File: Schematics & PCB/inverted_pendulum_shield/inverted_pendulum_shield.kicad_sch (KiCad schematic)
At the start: 6 parts, among them U1 AS78L05RTR-E1

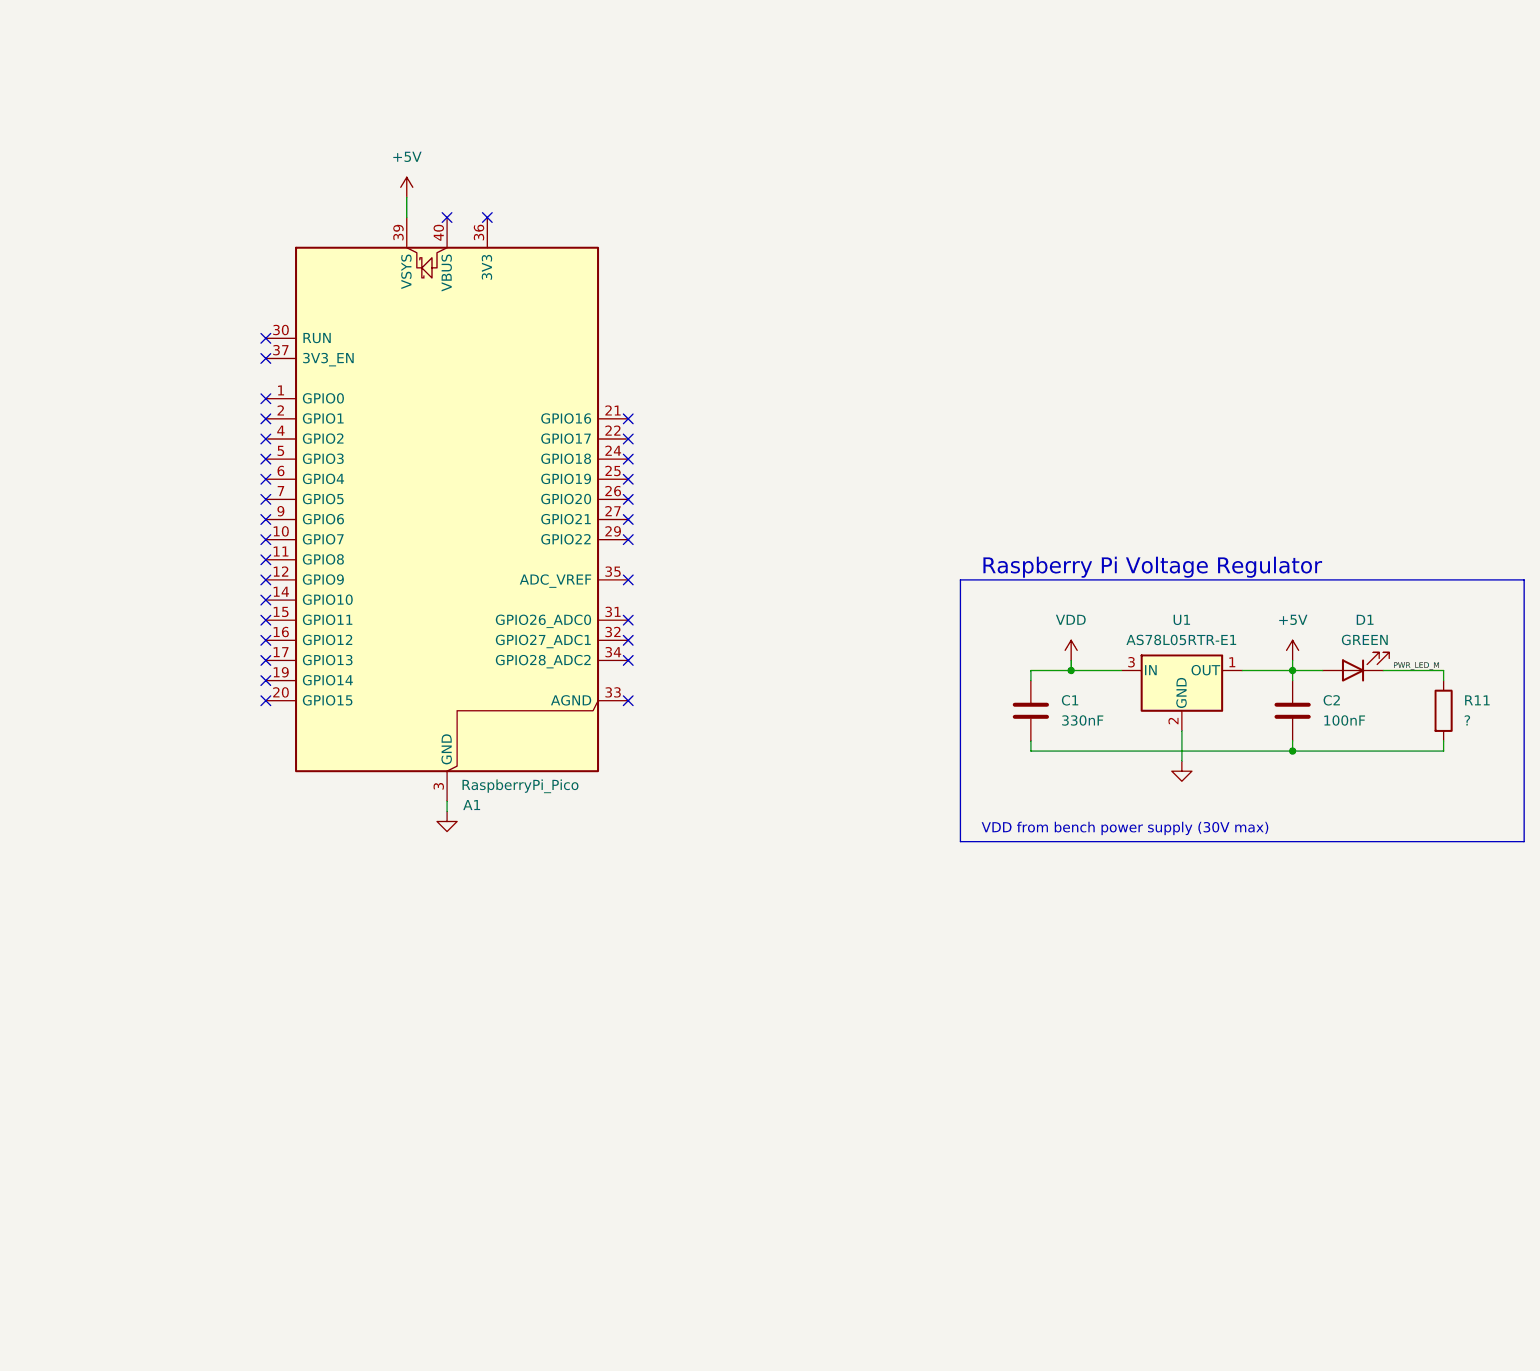
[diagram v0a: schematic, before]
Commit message: added reverse polarity protection
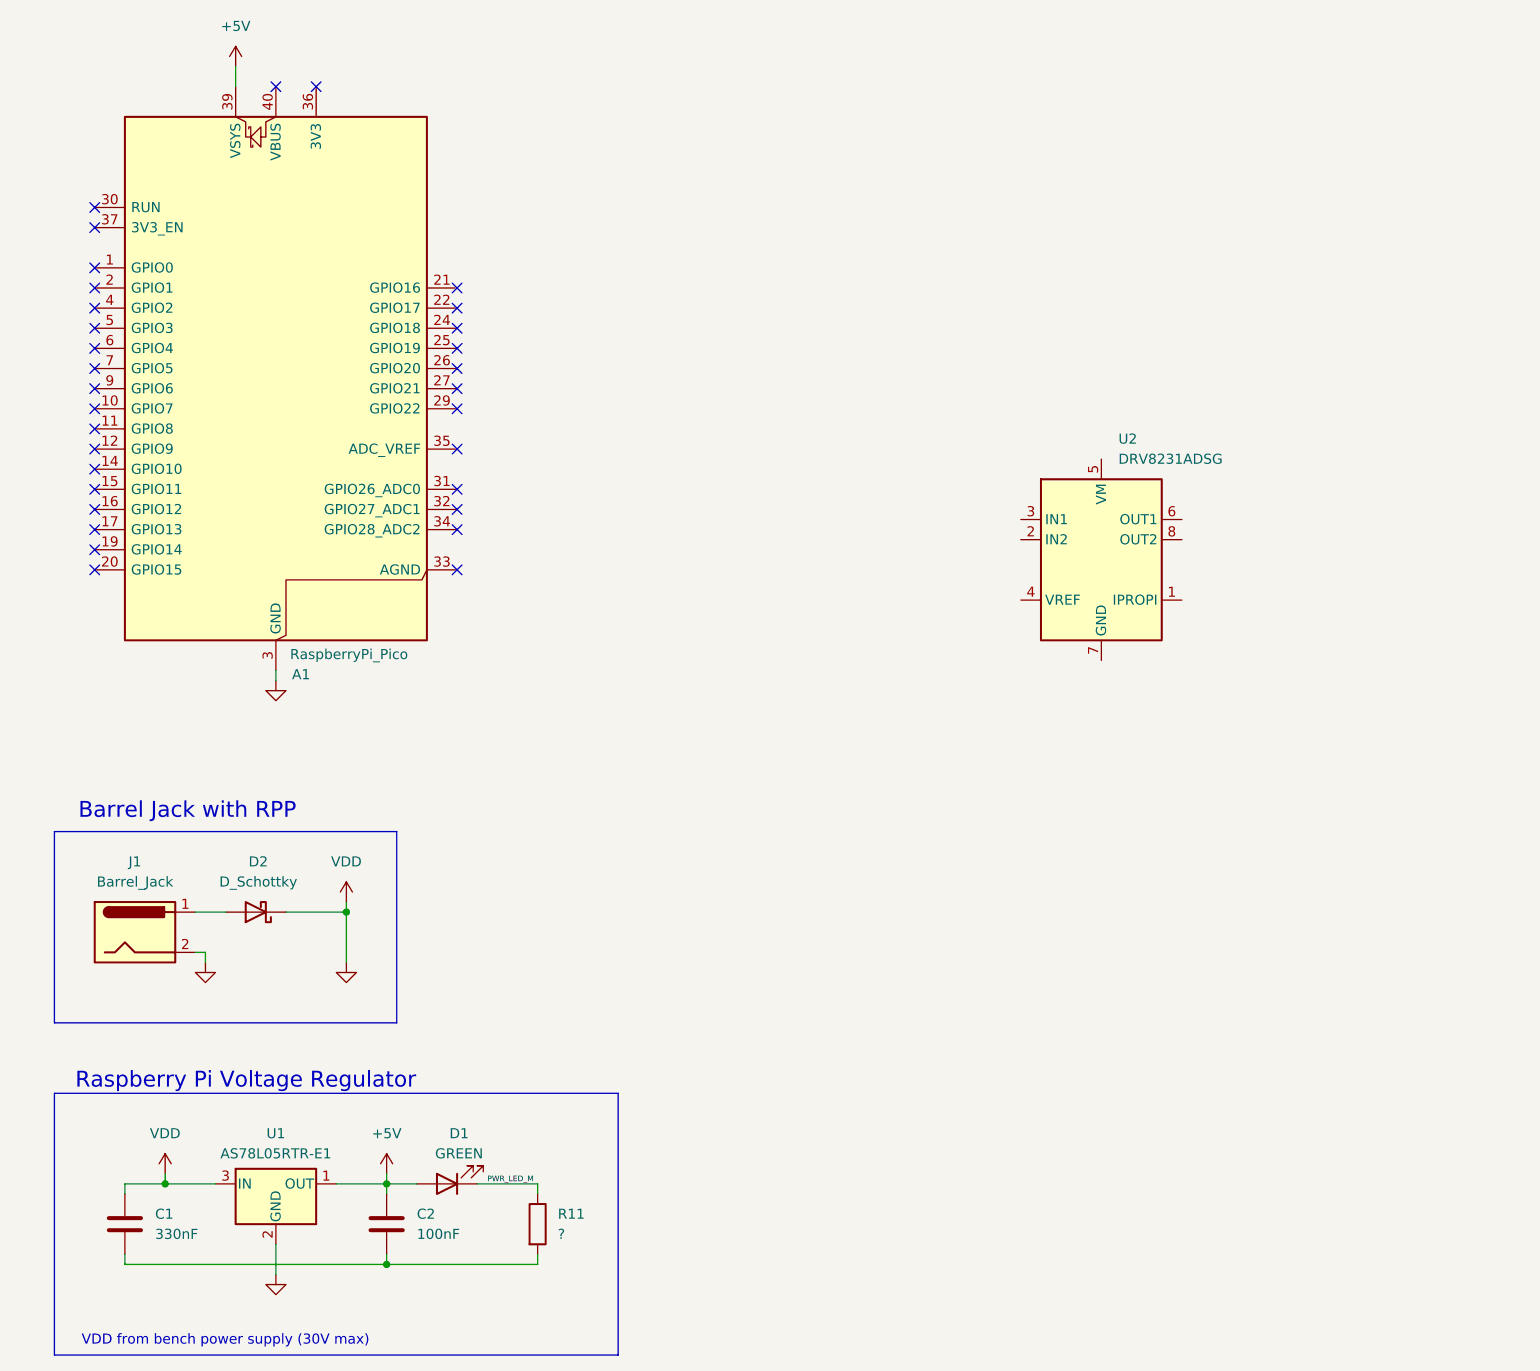
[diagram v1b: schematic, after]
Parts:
- added D2: D_Schottky, symbol Device:D_Schottky
- added J1: Barrel_Jack, symbol Connector:Barrel_Jack
- added U2: DRV8231ADSG, Package_SON:WSON-8-1EP_2x2mm_P0.5mm_EP0.9x1.6mm, symbol Driver_Motor:DRV8231ADSG
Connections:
- net VDD is gone; now on net GND: C1.1, U1.3 (IN)
- net GND: now also D2.1 (K), J1.2
- new net: U2.7 (GND), U2.9 (GND)
- new net: D2.2 (A), J1.1
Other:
- note added: "Barrel Jack with RPP"
- moved on the sheet: A1, C1, C2, D1, R11, U1

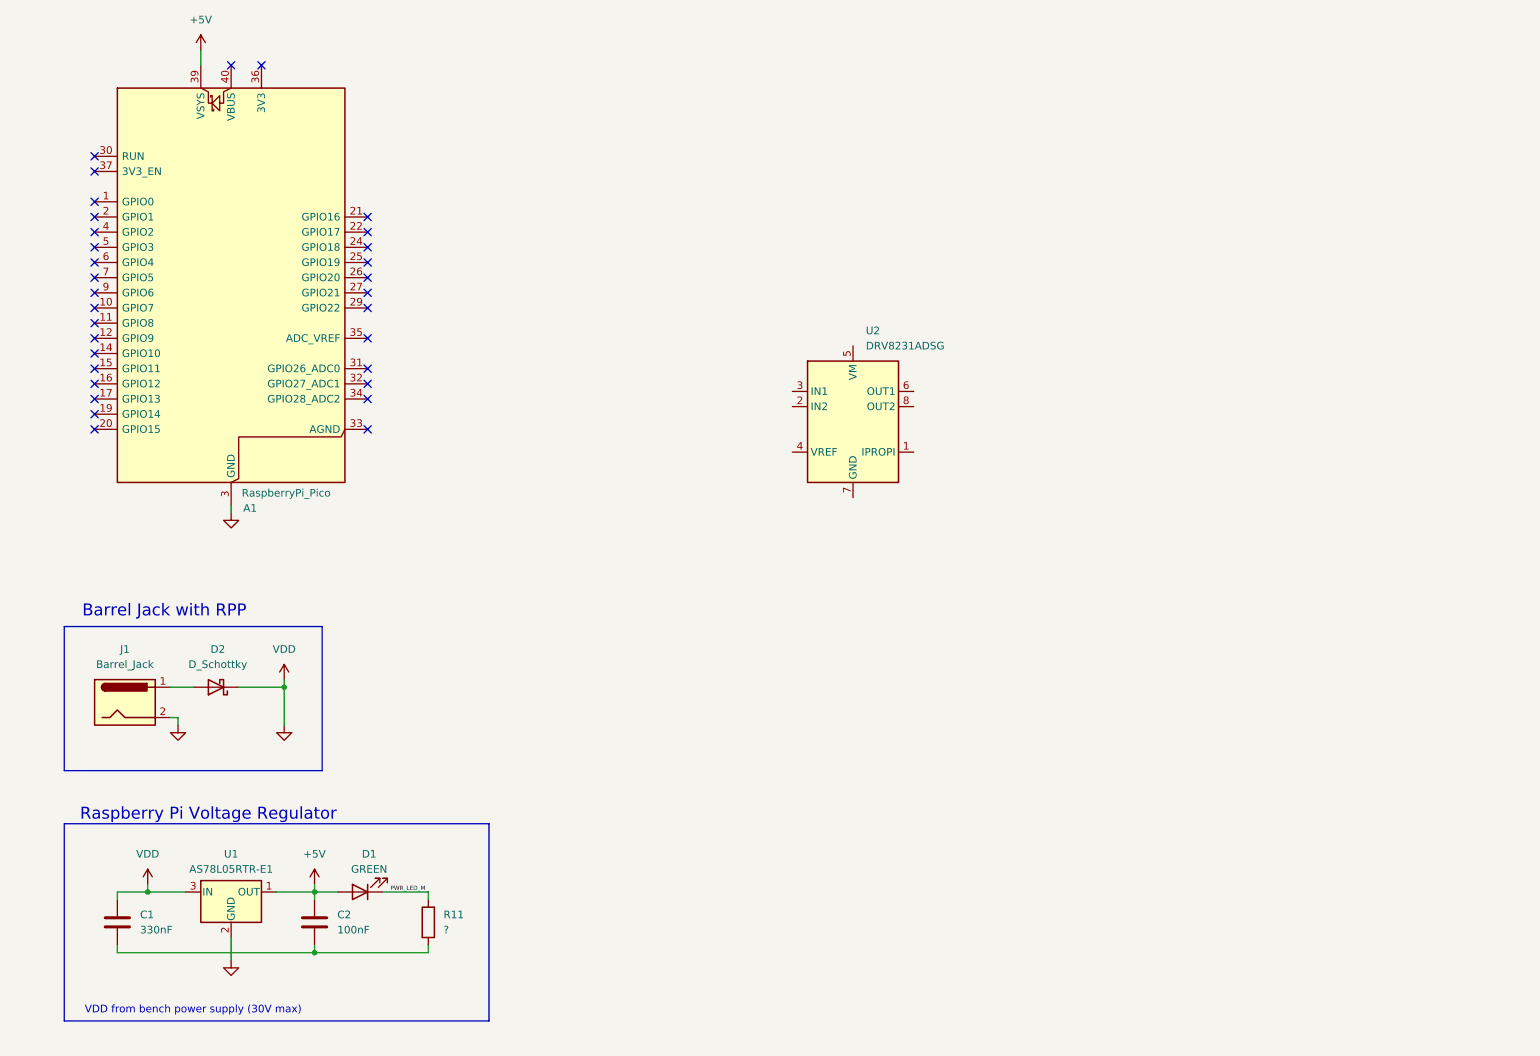
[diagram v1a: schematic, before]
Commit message: Added parts order and extra peripherals to shield
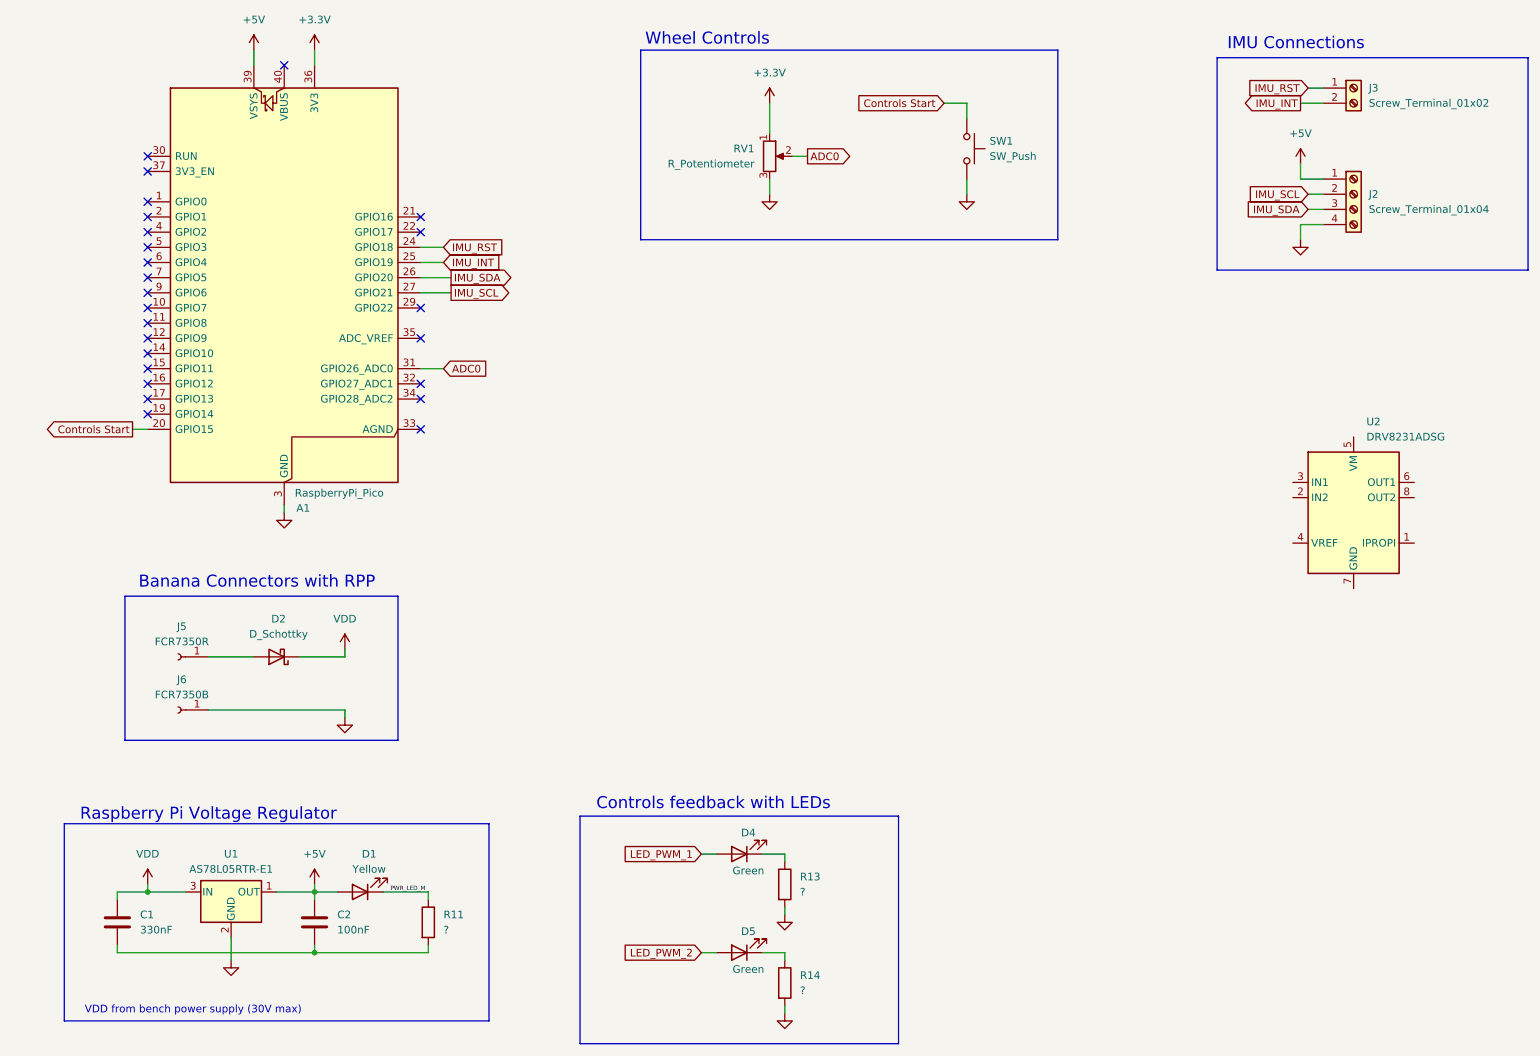
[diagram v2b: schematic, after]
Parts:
- removed J1: Barrel_Jack, symbol Connector:Barrel_Jack
- added D4, D5: Green, symbol Device:LED
- added J2: Screw_Terminal_01x04, symbol Connector:Screw_Terminal_01x04
- added J3: Screw_Terminal_01x02, symbol Connector:Screw_Terminal_01x02
- added J5: FCR7350R, symbol Connector:Conn_01x01_Socket
- added J6: FCR7350B, symbol Connector:Conn_01x01_Socket
- added R13, R14: ?, Resistor_SMD:R_0603_1608Metric, symbol Device:R
- added RV1: R_Potentiometer, symbol Device:R_Potentiometer
- added SW1: SW_Push, symbol Switch:SW_Push
- D1: value GREEN -> Yellow
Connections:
- net +5V: now also J2.1 (Pin_1)
- net GND: now also J2.4 (Pin_4), J6.1 (Pin_1), R13.2, R14.2, RV1.3, SW1.2; no longer C1.1, D2.1 (K), U1.3 (IN)
- net at D2.2 (A): now also J5.1 (Pin_1)
- net Controls Start: now reaches A1.20 (GPIO15)
- net Controls Start: now also SW1.1
- net IMU_RST: now reaches A1.24 (GPIO18)
- net IMU_RST: now also J3.1 (Pin_1)
- net IMU_INT: now reaches A1.25 (GPIO19)
- net IMU_INT: now also J3.2 (Pin_2)
- net IMU_SDA: now reaches A1.26 (GPIO20)
- net IMU_SDA: now also J2.3 (Pin_3)
- net IMU_SCL: now reaches A1.27 (GPIO21)
- net IMU_SCL: now also J2.2 (Pin_2)
- net ADC0: now reaches A1.31 (GPIO26_ADC0)
- net ADC0: now also RV1.2
- net +3.3V: now reaches A1.36 (3V3)
- net +3.3V: now also RV1.1
- new net: D5.1 (K), R14.1
- new net: D4.1 (K), R13.1
- new net LED_PWM_1: D4.2 (A)
- new net LED_PWM_2: D5.2 (A)
- new net VDD: C1.1, D2.1 (K), U1.3 (IN)
- no-connect marks 32 -> 25
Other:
- note added: "Banana Connectors with RPP"
- note added: "Controls feedback with LEDs"
- note added: "IMU Connections"
- note added: "Wheel Controls"
- note removed: "Barrel Jack with RPP"
- moved on the sheet: A1, D2, U2

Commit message: added the buck converters and H bridge
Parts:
- removed D1: Yellow, LED_SMD:LED_0603_1608Metric, symbol Device:LED
- removed D2: D_Schottky, symbol Device:D_Schottky
- removed R11: ?, Resistor_SMD:R_0603_1608Metric, symbol Device:R
- removed U1: AS78L05RTR-E1, Package_TO_SOT_SMD:SOT-89-3, symbol Regulator_Linear:L78L05_SOT89
- removed U2: DRV8231ADSG, Package_SON:WSON-8-1EP_2x2mm_P0.5mm_EP0.9x1.6mm, symbol Driver_Motor:DRV8231ADSG
- added C10, C6: 2x22uF, symbol Device:C
- added C3, C7: 10uF, symbol Device:C
- added C4: 47pF, symbol Device:C
- added C5, C8: 100nF, symbol Device:C
- added C9: 12pF, symbol Device:C
- added D3: D_Zener, symbol Device:D_Zener
- added J4: Screw_Terminal_01x02, symbol Connector:Screw_Terminal_01x02
- added L1: 6.8uH, symbol Device:L
- added L2: 10uH, symbol Device:L
- added Q1: PMOS, symbol Simulation_SPICE:PMOS
- added R12: 158k, Resistor_SMD:R_0603_1608Metric, symbol Device:R
- added R15, R16: 10k, Resistor_SMD:R_0603_1608Metric, symbol Device:R
- added R17: ?, Resistor_SMD:R_0603_1608Metric, symbol Device:R
- added R18: 1k, Resistor_SMD:R_0603_1608Metric, symbol Device:R
- added R19, R21: 30.1k, Resistor_SMD:R_0603_1608Metric, symbol Device:R
- added R20: 422k, Resistor_SMD:R_0603_1608Metric, symbol Device:R
- added R22: 0.18, Resistor_SMD:R_0603_1608Metric, symbol Device:R
- added U1: DRV8231DDAR, Package_SO:Texas_HTSOP-8-1EP_3.9x4.9mm_P1.27mm_EP2.95x4.9mm_Mask2.4x3.1mm_ThermalVias, symbol Driver_Motor:DRV8870DDA
- added U3, U4: AP63301WU-7, Package_TO_SOT_SMD:TSOT-23-6, symbol Regulator_Switching:AP63201WU
- C1: value 330nF -> 100nF
- C2: value 100nF -> 47uF
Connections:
- net +5V: now also C4.1, C6.1, L1.2, R12.1, R16.1, U1.4 (VREF); no longer C2.1
- net ADC0: now also R18.2; no longer RV1.2
- net Controls Start: now also R16.2
- net GND: now also C1.2, C2.2, C10.2, C3.2, C6.2, C7.2, R15.2, R17.2, R19.2, R21.2, R22.2, U1.1 (GND), U1.9 (GND), U3.4 (GND), U4.4 (GND); no longer RV1.3
- net LED_PWM_1: now also A1.16 (GPIO12)
- net LED_PWM_2: now also A1.17 (GPIO13)
- net VDD: now also C3.1, C7.1, D3.1 (K), Q1.3 (S), U3.2 (EN), U3.3 (IN), U4.2 (EN), U4.3 (IN); no longer C1.1
- net at J5.1 (Pin_1): now also Q1.1 (D)
- net Motor Control 1: now reaches A1.1 (GPIO0)
- net Motor Control 1: now also U1.3 (IN1)
- net Motor Control 2: now reaches A1.2 (GPIO1)
- net Motor Control 2: now also U1.2 (IN2)
- new net: C9.2, R20.2, R21.1, U4.1 (FB)
- new net: C4.2, R12.2, R19.1, U3.1 (FB)
- new net: C5.1, L1.1, U3.5 (SW)
- new net: C5.2, U3.6 (BST)
- new net: R22.1, U1.7 (ISEN)
- new net: D3.2 (A), Q1.2 (G), R17.1
- new net: R18.1, RV1.2
- new net: C8.1, L2.1, U4.5 (SW)
- new net: C8.2, U4.6 (BST)
- new net: R15.1, RV1.3
- new net +12V: C1.1, C10.1, C2.1, C9.1, L2.2, R20.1, U1.5 (VM)
- new net OUT1: J4.1 (Pin_1), U1.6 (OUT1)
- new net OUT2: J4.2 (Pin_2), U1.8 (OUT2)
- no-connect marks 25 -> 21
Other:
- note added: "Current is regulated at 2.78A = VREF / (10 * 0.18)"
- note added: "H-Bridge Buck Converter"
- note added: "Might need higher in case of H bridge Vdrop"
- note added: "Raspberry Pi Buck Converter"
- note removed: "Raspberry Pi Voltage Regulator"
- moved on the sheet: A1, D4, D5, J2, J3, J5, J6, R13, R14, RV1, SW1
